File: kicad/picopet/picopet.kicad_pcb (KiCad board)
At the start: 2 copper layers, 11 parts, among them J1 USB_C_Receptacle_G-Switch_GT-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, U2 W25Q128JVS, U3 RP2040, Y1 ABLS-12.000MHZ-B4-T

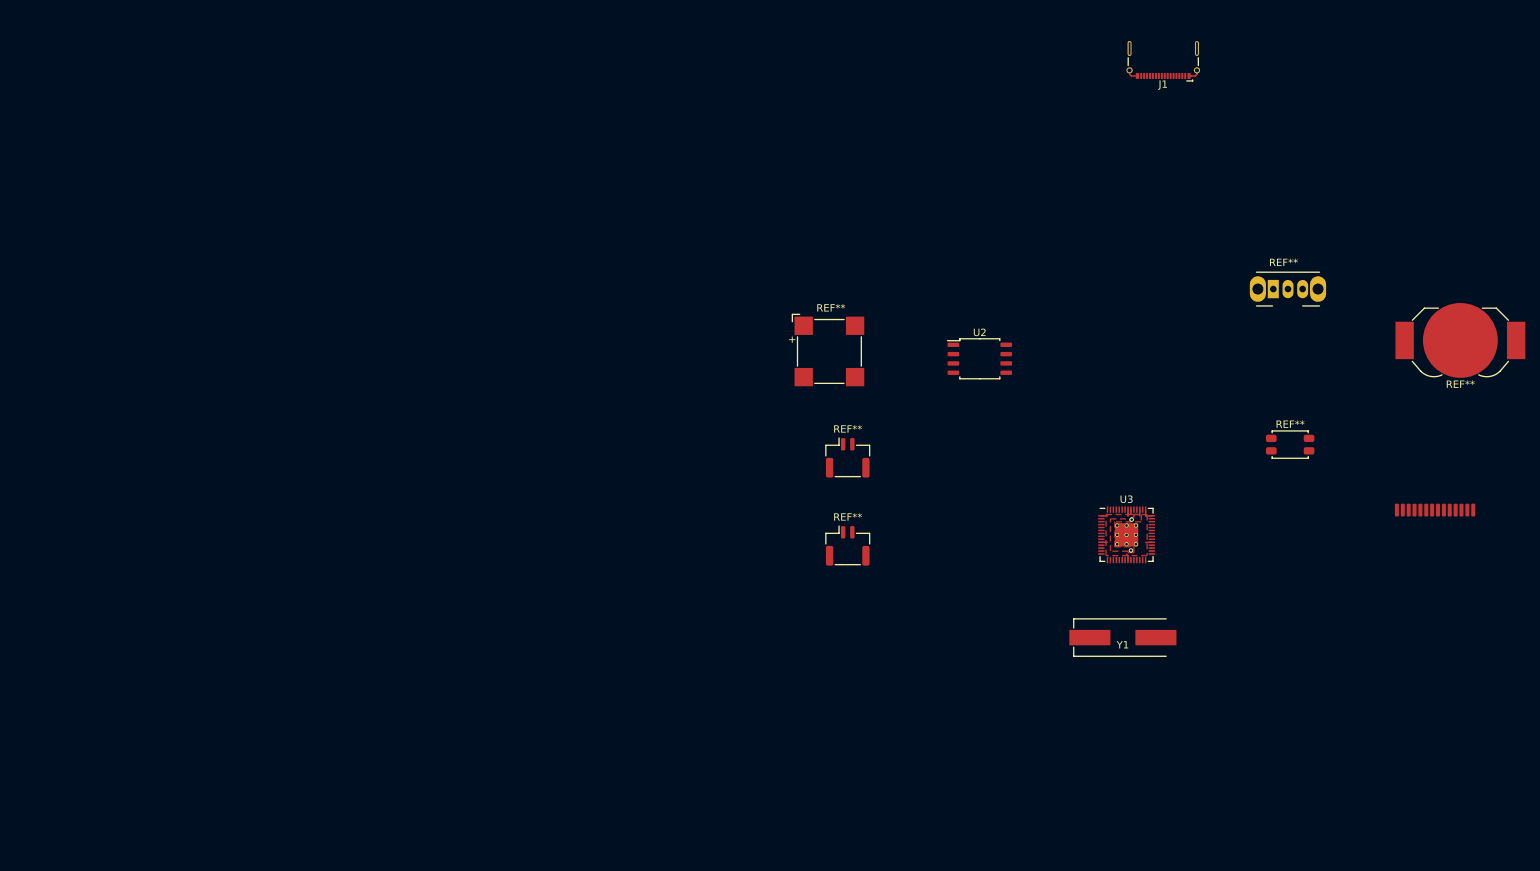
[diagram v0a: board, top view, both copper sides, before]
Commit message: Working on a PCB layout, but didn't plan the LCD well enough
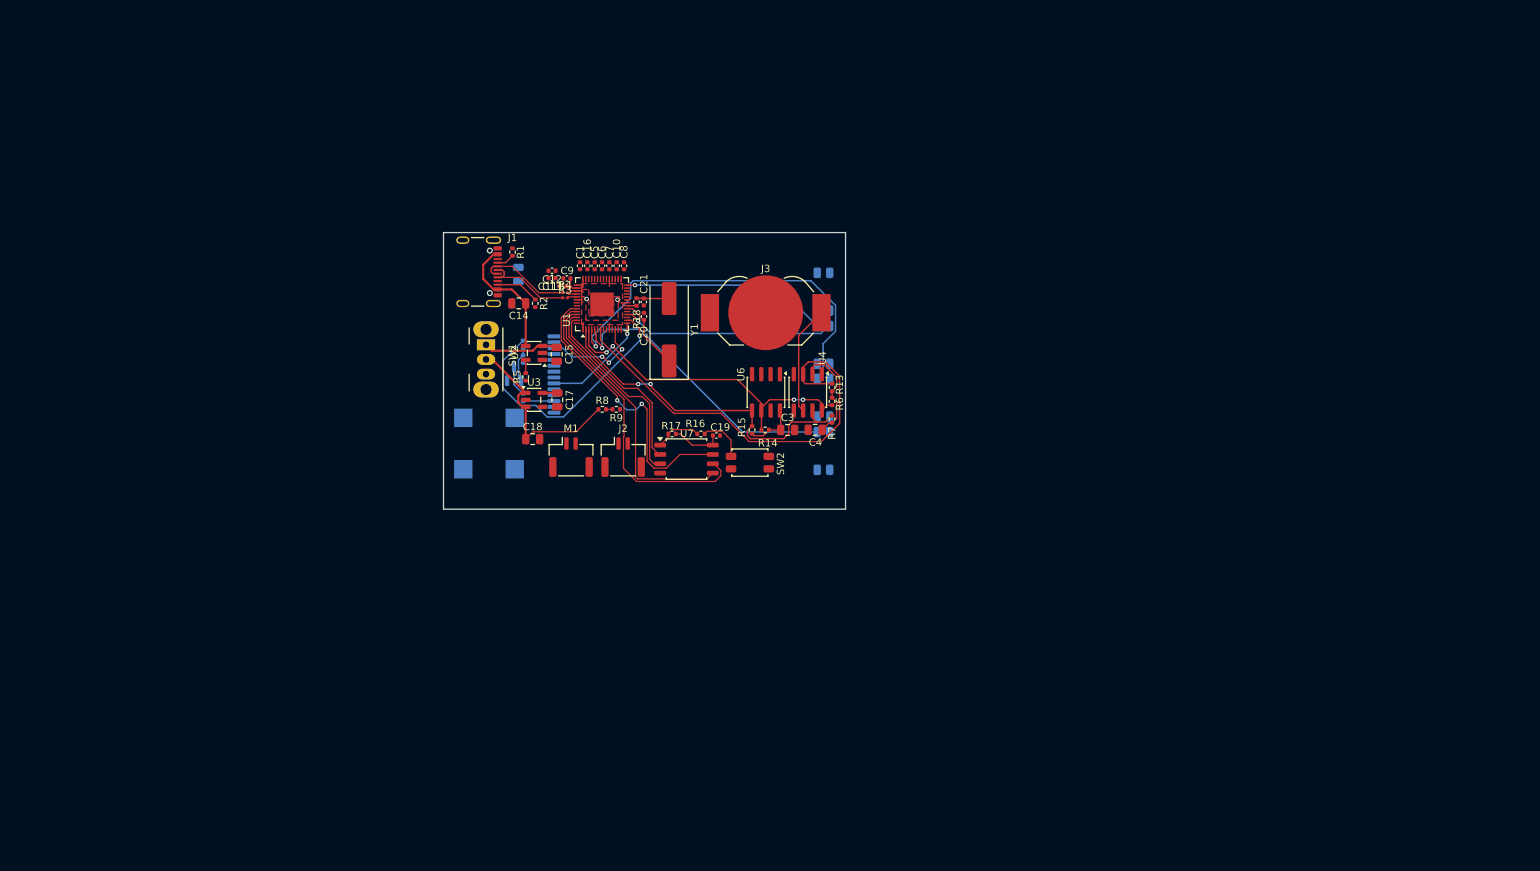
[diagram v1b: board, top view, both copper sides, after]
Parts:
- removed REF** (x2): JST_GH_SM02B-GHS-TB_1x02-1MP_P1.25mm_Horizontal, Connector_JST:JST_GH_SM02B-GHS-TB_1x02-1MP_P1.25mm_Horizontal
- removed REF**: ST7735_P0.8mm, custom:ST7735_P0.8mm
- removed REF**: MagneticBuzzer_CUI_CMT-8504-100-SMT, Buzzer_Beeper:MagneticBuzzer_CUI_CMT-8504-100-SMT
- removed REF**: SW_Slide_SPDT_Angled_CK_OS102011MA1Q, Button_Switch_THT:SW_Slide_SPDT_Angled_CK_OS102011MA1Q
- removed REF**: SW_SPST_EVQP2_MiddlePushTravel_H2.5mm, Button_Switch_SMD:SW_SPST_EVQP2_MiddlePushTravel_H2.5mm
- removed REF**: BatteryHolder_LINX_BAT-HLD-012-SMT, Battery:BatteryHolder_LINX_BAT-HLD-012-SMT
- added BZ1: Buzzer, Buzzer_Beeper:MagneticBuzzer_CUI_CMT-8504-100-SMT, B.Cu at (78.6, 77.1)
- added C1: 100n, Capacitor_SMD:C_0402_1005Metric, F.Cu at (91.0, 52.8)
- added C10: 100n, Capacitor_SMD:C_0402_1005Metric, F.Cu at (96.0, 52.8)
- added C11: 1u, Capacitor_SMD:C_0402_1005Metric, F.Cu at (88.7, 55.6)
- added C12: 100n, Capacitor_SMD:C_0402_1005Metric, F.Cu at (87.2, 53.5)
- added C13: 100n, Capacitor_SMD:C_0402_1005Metric, F.Cu at (87.2, 54.5)
- added C14: 4.7u, Capacitor_SMD:C_0805_2012Metric, F.Cu at (82.7, 58.0)
- added C15: 4.7u, Capacitor_SMD:C_0805_2012Metric, F.Cu at (87.8, 64.9)
- added C16: 100n, Capacitor_SMD:C_0402_1005Metric, F.Cu at (92.0, 52.8)
- added C17: 1u, Capacitor_SMD:C_0805_2012Metric, F.Cu at (87.9, 71.1)
- added C18: 1u, Capacitor_SMD:C_0805_2012Metric, F.Cu at (84.6, 76.5)
- added C19: 100n, Capacitor_SMD:C_0402_1005Metric, F.Cu at (109.6, 76.0)
- added C2: 1u, Capacitor_SMD:C_0805_2012Metric, B.Cu at (82.6, 54.0)
- added C20: 27p, Capacitor_SMD:C_0402_1005Metric, F.Cu at (99.7, 59.7)
- added C21: 27p, Capacitor_SMD:C_0402_1005Metric, F.Cu at (99.7, 57.8)
- added C3: 4.7u, Capacitor_SMD:C_0805_2012Metric, F.Cu at (119.3, 75.2)
- added C4: 4.7u, Capacitor_SMD:C_0805_2012Metric, F.Cu at (123.1, 75.2)
- added C5: 100n, Capacitor_SMD:C_0402_1005Metric, F.Cu at (93.0, 52.8)
- added C6: 100n, Capacitor_SMD:C_0402_1005Metric, F.Cu at (94.0, 52.8)
- added C7: 100n, Capacitor_SMD:C_0402_1005Metric, F.Cu at (95.0, 52.8)
- added C8: 100n, Capacitor_SMD:C_0402_1005Metric, F.Cu at (97.0, 52.8)
- added C9: 1u, Capacitor_SMD:C_0402_1005Metric, F.Cu at (89.2, 54.6)
- added J2: MicroJST 1.25mm female, Connector_JST:JST_GH_SM02B-GHS-TB_1x02-1MP_P1.25mm_Horizontal, F.Cu at (96.9, 78.9)
- added J3: CR1220 Holder, Battery:BatteryHolder_LINX_BAT-HLD-012-SMT, F.Cu at (116.3, 59.2)
- added J4: ST7735 LCD, custom:ST7735_P0.8mm, B.Cu at (102.1, 67.7)
- added M1: Motor_DC, Connector_JST:JST_GH_SM02B-GHS-TB_1x02-1MP_P1.25mm_Horizontal, F.Cu at (89.8, 78.9)
- added Q1: SS8050, Package_TO_SOT_SMD:SOT-23, B.Cu at (82.0, 67.5)
- added R1: 5K1, Resistor_SMD:R_0402_1005Metric, F.Cu at (81.8, 51.0)
- added R10: 10, Resistor_SMD:R_0402_1005Metric, B.Cu at (83.2, 70.8)
- added R11: 10K, Resistor_SMD:R_0402_1005Metric, B.Cu at (83.2, 65.5)
- added R12: 1K, Resistor_SMD:R_0402_1005Metric, B.Cu at (83.2, 63.5)
- added R13: 5K1, Resistor_SMD:R_0402_1005Metric, F.Cu at (125.4, 69.4)
- added R14: 5K1, Resistor_SMD:R_0402_1005Metric, F.Cu at (116.2, 75.2)
- added R15: 5K1, Resistor_SMD:R_0402_1005Metric, F.Cu at (114.5, 75.2)
- added R16: 1k, Resistor_SMD:R_0402_1005Metric, F.Cu at (107.5, 75.7)
- added R17: DNF, Resistor_SMD:R_0402_1005Metric, F.Cu at (103.5, 75.7)
- added R18: 1k, Resistor_SMD:R_0402_1005Metric, F.Cu at (98.7, 57.8)
- added R2: 5K1, Resistor_SMD:R_0402_1005Metric, F.Cu at (84.9, 57.9)
- added R3: 27, Resistor_SMD:R_0201_0603Metric, F.Cu at (89.0, 57.2)
- added R4: 27, Resistor_SMD:R_0201_0603Metric, F.Cu at (89.0, 56.5)
- added R5: 5K1, Resistor_SMD:R_0402_1005Metric, F.Cu at (83.6, 68.0)
- added R6: 5K1, Resistor_SMD:R_0402_1005Metric, F.Cu at (125.4, 71.3)
- added R7: 5K1, Resistor_SMD:R_0402_1005Metric, F.Cu at (125.4, 73.7)
- added R8: 100k, Resistor_SMD:R_0402_1005Metric, F.Cu at (94.0, 72.4)
- added R9: 100k, Resistor_SMD:R_0402_1005Metric, F.Cu at (95.9, 72.4)
- added SW1: PWR, Button_Switch_THT:SW_Slide_SPDT_Angled_CK_OS102011MA1Q, F.Cu at (78.2, 63.6)
- added SW2: BOOTSEL, Button_Switch_SMD:SW_SPST_EVQP2_MiddlePushTravel_H2.5mm, F.Cu at (114.2, 79.7)
- added SW4: Btn0, Button_Switch_SMD:SW_SPST_EVQP2_MiddlePushTravel_H2.5mm, B.Cu at (124.2, 56.4)
- added SW5: Btn1, Button_Switch_SMD:SW_SPST_EVQP2_MiddlePushTravel_H2.5mm, B.Cu at (124.2, 63.6)
- added SW6: Btn2, Button_Switch_SMD:SW_SPST_EVQP2_MiddlePushTravel_H2.5mm, B.Cu at (124.2, 70.8)
- added SW7: Btn3, Button_Switch_SMD:SW_SPST_EVQP2_MiddlePushTravel_H2.5mm, B.Cu at (124.2, 78.1)
- added U1: RP2040, Package_DFN_QFN:QFN-56-1EP_7x7mm_P0.4mm_EP3.2x3.2mm, F.Cu at (94.0, 58.1)
- added U4: DS3231MZ, Package_SO:SOIC-8_3.9x4.9mm_P1.27mm, F.Cu at (122.1, 70.1)
- added U6: AT24CS32-SSHM, Package_SO:SOIC-8_3.9x4.9mm_P1.27mm, F.Cu at (116.4, 70.1)
- added U7: W25Q128JVS, Package_SO:SOIC-8_5.3x5.3mm_P1.27mm, F.Cu at (105.5, 79.2)
- J1: value USB_C_Receptacle_G-Switch_GT-USB-7025 -> USB_C_Receptacle_USB2.0_14P; footprint Connector_USB:USB_C_Receptacle_G-Switch_GT-USB-7025 -> Connector_USB:USB_C_Receptacle_GCT_USB4105-xx-A_16P_TopMnt_Horizontal
- U2: value W25Q128JVS -> MCP73831-2-OT; footprint Package_SO:SOIC-8_5.23x5.23mm_P1.27mm -> Package_TO_SOT_SMD:SOT-23-5
- U3: value RP2040 -> S-T111B33MC-OGSTFU; footprint RP2040_minimal:RP2040-QFN-56 -> Package_TO_SOT_SMD:SOT-23-5
- Y1: footprint RP2040_minimal:Crystal_SMD_HC49-US -> Crystal:Crystal_SMD_HC49-SD
- moved J1 99.1 mm to (76.1, 53.7), turned to -90 degrees
- moved U3 82.8 mm to (84.7, 71.1)
- moved Y1 74.7 mm to (103.2, 61.5), turned to 90 degrees
- moved U2 60.8 mm to (84.7, 64.7), turned to 180 degrees
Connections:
- J1 pad A1: (no net) -> GND
- J1 pad A12: (no net) -> GND
- J1 pad A4: (no net) -> Net-(U2-V_{DD})
- J1 pad A5: (no net) -> Net-(J1-CC1)
- J1 pad A6: (no net) -> USB_D+
- J1 pad A7: (no net) -> USB_D-
- J1 pad A9: (no net) -> Net-(U2-V_{DD})
- J1 pad B1: (no net) -> GND
- J1 pad B12: (no net) -> GND
- J1 pad B4: (no net) -> Net-(U2-V_{DD})
- J1 pad B5: (no net) -> Net-(J1-CC2)
- J1 pad B6: (no net) -> USB_D+
- J1 pad B7: (no net) -> USB_D-
- J1 pad B9: (no net) -> Net-(U2-V_{DD})
- J1 pad S1: (no net) -> GND
- U2 pad 1: (no net) -> GPIO_UNDECIDE_A
- U2 pad 2: (no net) -> GND
- U2 pad 3: (no net) -> VBAT
- U2 pad 4: (no net) -> Net-(U2-V_{DD})
- U2 pad 5: (no net) -> Net-(U2-PROG)
- U3 pad 1: (no net) -> VSENSE
- U3 pad 2: (no net) -> GND
- U3 pad 3: (no net) -> VSENSE
- U3 pad 4: (no net) -> GND
- U3 pad 5: (no net) -> +3V3
- Y1 pad 1: (no net) -> /XIN
- Y1 pad 2: (no net) -> Net-(C21-Pad1)
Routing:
- net GPIO5: track 0.00 -> 59.3 mm
- net GPIO2: track 0.00 -> 54.1 mm, vias 0 -> 1
- net GPIO0: track 0.00 -> 48.1 mm, vias 0 -> 2
- net GPIO1: track 0.00 -> 45.3 mm, vias 0 -> 4
- net /QSPI_SCLK: track 0.00 -> 42.5 mm
- net GPIO3: track 0.00 -> 40.2 mm, vias 0 -> 1
- net /QSPI_SD3: track 0.00 -> 39.5 mm, vias 0 -> 2
- net /QSPI_SD0: track 0.00 -> 38.0 mm
- net GPIO13: track 0.00 -> 36.0 mm, vias 0 -> 1
- net +3V3: track 6.98 -> 40.0 mm
- net GPIO15: track 0.00 -> 31.0 mm, vias 0 -> 1
- net GPIO17: track 0.00 -> 28.2 mm, vias 0 -> 1
- net /QSPI_SD2: track 0.00 -> 27.5 mm
- net VSENSE: track 0.00 -> 25.7 mm
- net /QSPI_SD1: track 0.00 -> 25.1 mm
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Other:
- board outline added: 54.8 x 37.7 mm

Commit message: Redesigning pcb
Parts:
- removed M1: Motor_DC, Connector_JST:JST_GH_SM02B-GHS-TB_1x02-1MP_P1.25mm_Horizontal
- removed R16, R18: 1k, Resistor_SMD:R_0402_1005Metric
- removed R17: DNF, Resistor_SMD:R_0402_1005Metric
- removed SW7: Btn3, Button_Switch_SMD:SW_SPST_EVQP2_MiddlePushTravel_H2.5mm
- added J5: ST7735 LCD, custom:ST7735_P0.8mm, F.Cu at (115.4, 58.5)
- added SW3: Btn0, Button_Switch_SMD:SW_SPST_EVQP2_MiddlePushTravel_H2.5mm, F.Cu at (105.1, 65.4)
- BZ1, Q1: moved to F.Cu
- C11: value 1u -> 100n
- C12, C13: value 100n -> 15p
- C14, C3, C4: value 4.7u -> 100n; footprint Capacitor_SMD:C_0805_2012Metric -> Capacitor_SMD:C_0402_1005Metric
- C15: value 4.7u -> 2u2; footprint Capacitor_SMD:C_0805_2012Metric -> Capacitor_SMD:C_0402_1005Metric
- C16, C8: value 100n -> 1u
- C19: value 100n -> 4.7u; footprint Capacitor_SMD:C_0402_1005Metric -> Capacitor_SMD:C_0805_2012Metric
- C2: value 1u -> 100n; footprint Capacitor_SMD:C_0805_2012Metric -> Capacitor_SMD:C_0402_1005Metric; moved to F.Cu
- C20, C21: value 27p -> 4.7u; footprint Capacitor_SMD:C_0402_1005Metric -> Capacitor_SMD:C_0805_2012Metric
- J2: value MicroJST 1.25mm female -> PH1.25mm 2P
- J3: value CR1220 Holder -> PH1.25mm 2P; footprint Battery:BatteryHolder_LINX_BAT-HLD-012-SMT -> Connector_JST:JST_GH_SM02B-GHS-TB_1x02-1MP_P1.25mm_Horizontal
- J4: value ST7735 LCD -> CR1220 Holder; footprint custom:ST7735_P0.8mm -> Battery:BatteryHolder_LINX_BAT-HLD-012-SMT; moved to F.Cu
- R1, R2: value 5K1 -> 27; footprint Resistor_SMD:R_0402_1005Metric -> Resistor_SMD:R_0201_0603Metric
- R10: value 10 -> 5k1; footprint Resistor_SMD:R_0402_1005Metric -> Resistor_SMD:R_0201_0603Metric; moved to F.Cu
- R11: value 10K -> 5k1; footprint Resistor_SMD:R_0402_1005Metric -> Resistor_SMD:R_0201_0603Metric; moved to F.Cu
- R12: value 1K -> 5k1; footprint Resistor_SMD:R_0402_1005Metric -> Resistor_SMD:R_0201_0603Metric; moved to F.Cu
- R13, R14, R15: footprint Resistor_SMD:R_0402_1005Metric -> Resistor_SMD:R_0201_0603Metric
- R3: value 27 -> 1k; footprint Resistor_SMD:R_0201_0603Metric -> Resistor_SMD:R_0402_1005Metric
- R4: value 27 -> 1k
- R5: value 5K1 -> 10; footprint Resistor_SMD:R_0402_1005Metric -> Resistor_SMD:R_0201_0603Metric
- R6: value 5K1 -> 10k; footprint Resistor_SMD:R_0402_1005Metric -> Resistor_SMD:R_0201_0603Metric
- R7: value 5K1 -> 1k; footprint Resistor_SMD:R_0402_1005Metric -> Resistor_SMD:R_0201_0603Metric
- SW1: footprint Button_Switch_THT:SW_Slide_SPDT_Angled_CK_OS102011MA1Q -> Button_Switch_SMD:SW_SPDT_CK_JS102011SAQN
- SW4: value Btn0 -> Btn1; moved to F.Cu
- SW5: value Btn1 -> Btn2; moved to F.Cu
- SW6: value Btn2 -> Btn3; moved to F.Cu
- U7: value W25Q128JVS -> W25Q32JVSSIQ; footprint Package_SO:SOIC-8_5.3x5.3mm_P1.27mm -> Package_SO:SOIC-8-1EP_3.9x4.9mm_P1.27mm_EP2.29x3mm
- Y1: value ABLS-12.000MHZ-B4-T -> X322512MSB4SI; footprint Crystal:Crystal_SMD_HC49-SD -> Crystal:Crystal_SMD_3225-4Pin_3.2x2.5mm
- moved C4 99.4 mm to (28.0, 46.0), turned to 0 degrees
- moved C3 95.0 mm to (27.5, 50.5)
- moved C20 89.3 mm to (36.1, 122.4), turned to 180 degrees
- moved C19 89.3 mm to (32.8, 121.5), turned to -90 degrees
- moved J4 88.7 mm to (179.1, 23.7), turned to 0 degrees
- moved SW2 87.7 mm to (30.6, 52.8), turned to 90 degrees
- moved J1 83.1 mm to (39.5, 128.3), turned to 0 degrees
- moved SW1 82.0 mm to (29.0, 129.2), turned to 0 degrees
- moved J2 80.4 mm to (28.4, 121.1), turned to -90 degrees
- moved R9 77.7 mm to (28.9, 111.6)
- moved R8 77.7 mm to (27.0, 111.6)
- moved C8 77.2 mm to (19.8, 52.1), turned to -90 degrees
- moved C7 77.1 mm to (18.0, 50.5), turned to 180 degrees
- moved C6 76.7 mm to (17.6, 46.0), turned to 180 degrees
- moved C10 74.7 mm to (22.2, 41.2)
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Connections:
- net GPIO_UNDECIDE_B renamed GPIO26
- C10 pad 1: +3V3 -> +1V1
- C12 pad 1: +1V1 -> /XIN
- C13 pad 1: +1V1 -> Net-(C13-Pad1)
- C14 pad 1: Net-(U2-V_{DD}) -> +3V3
- C15 pad 1: VBAT -> GND
- C15 pad 2: GND -> +3V3
- C16 pad 1: +3V3 -> GND
- C16 pad 2: GND -> +3V3
- C19 pad 1: +3V3 -> VBAT
- C20 pad 1: /XIN -> USBC_VDD
- C21 pad 1: Net-(C21-Pad1) -> +3V3
- C9 pad 1: +3V3 -> +1V1
- J1 pad A4: Net-(U2-V_{DD}) -> USBC_VDD
- J1 pad A9: Net-(U2-V_{DD}) -> USBC_VDD
- J1 pad B4: Net-(U2-V_{DD}) -> USBC_VDD
- J1 pad B9: Net-(U2-V_{DD}) -> USBC_VDD
- J3 pad 1: VCOIN -> GND
- J3 pad 2: GND -> GPIO6
- J4 pad 1: (no net) -> VCOIN
- R1 pad 1: Net-(J1-CC1) -> USB_D+
- R1 pad 2: GND -> Net-(U1-USB_DP)
- R10 pad 1: Net-(J4-LED-) -> Net-(J1-CC1)
- R10 pad 2: Net-(Q1-C) -> GND
- R11 pad 1: +3V3 -> Net-(J1-CC2)
- R11 pad 2: Net-(Q1-B) -> GND
- R12 pad 1: Net-(Q1-B) -> GND
- R12 pad 2: GPIO13 -> Net-(U2-PROG)
- R2 pad 1: Net-(J1-CC2) -> USB_D-
- R2 pad 2: GND -> Net-(U1-USB_DM)
- R3 pad 1: USB_D+ -> /XOUT
- R3 pad 2: Net-(U1-USB_DP) -> Net-(C13-Pad1)
- R4 pad 1: USB_D- -> /QSPI_SS
- R4 pad 2: Net-(U1-USB_DM) -> Net-(R4-Pad2)
- R5 pad 1: GND -> Net-(Q1-C)
- R5 pad 2: Net-(U2-PROG) -> Net-(J5-LED-)
- R6 pad 1: GPIO1 -> Net-(Q1-B)
- R7 pad 1: GPIO0 -> GPIO13
- R7 pad 2: +3V3 -> Net-(Q1-B)
- SW1 pad 1: VBAT -> VSENSE
- SW1 pad 2: VSENSE -> VBAT
- SW1 pad 3: (no net) -> unconnected-(SW1-C-Pad3)
- SW2 pad 1: GND -> Net-(R4-Pad2)
- SW2 pad 2: Net-(R16-Pad2) -> GND
- SW4 pad 1: GPIO15 -> GPIO17
- SW5 pad 1: GPIO17 -> GPIO2
- SW6 pad 1: GPIO2 -> GPIO3
- U1 pad 37: /GPIO25 -> GPIO25
- U2 pad 1: GPIO_UNDECIDE_A -> GPIO25
- U2 pad 4: Net-(U2-V_{DD}) -> USBC_VDD
- Y1 pad 2: Net-(C21-Pad1) -> Net-(C13-Pad1)
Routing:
- net GPIO5: track 59.3 -> 1.96 mm
- net GPIO2: track 54.1 -> 0.00 mm, vias 1 -> 0
- net GPIO3: track 40.2 -> 0.00 mm, vias 1 -> 0
- net GPIO13: track 36.0 -> 0.00 mm, vias 1 -> 0
- net GPIO0: track 48.1 -> 14.1 mm, vias 2 -> 0
- net GPIO1: track 45.3 -> 11.8 mm, vias 4 -> 0
- net GPIO15: track 31.0 -> 0.00 mm, vias 1 -> 0
- net GPIO17: track 28.2 -> 0.00 mm, vias 1 -> 0
- net /QSPI_SD0: track 38.0 -> 17.5 mm
- net /QSPI_SCLK: track 42.5 -> 22.6 mm
- net +3V3: track 40.0 -> 21.3 mm
- net Net-(U2-V_{DD}): track 17.5 -> 0.00 mm
- net /QSPI_SD2: track 27.5 -> 11.1 mm
- net VCOIN: track 14.9 -> 0.00 mm
- net /QSPI_SD1: track 25.1 -> 10.3 mm
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- removed copper zone on F.Cu, net +1V1
- removed copper zone on F.Cu, net +3V3
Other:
- board outline removed

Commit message: Redesigning pcb
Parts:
- J5, SW3, SW4, SW5, SW6: moved to B.Cu
- U7: footprint Package_SO:SOIC-8-1EP_3.9x4.9mm_P1.27mm_EP2.29x3mm -> Package_SO:SOIC-8_3.9x4.9mm_P1.27mm
- moved Y1 108.7 mm to (27.8, 36.3), turned to 180 degrees
- moved J4 106.1 mm to (75.0, 44.3), turned to 90 degrees
- moved C13 105.9 mm to (25.2, 35.9), turned to -90 degrees
- moved J3 101.7 mm to (33.9, 45.1), turned to 180 degrees
- moved BZ1 100.9 mm to (49.9, 126.9), turned to -90 degrees
- moved R3 99.3 mm to (24.2, 36.0), turned to 90 degrees
- moved C12 98.6 mm to (30.4, 35.9), turned to -90 degrees
- moved C21 95.2 mm to (69.1, 52.2)
- moved R13 95.2 mm to (60.1, 46.1)
- moved R14 95.2 mm to (67.3, 43.5)
- moved R15 95.2 mm to (69.1, 50.1)
- moved U4 95.2 mm to (64.3, 46.4)
- moved U6 95.2 mm to (64.3, 51.9)
- moved C14 91.6 mm to (39.3, 49.0), turned to 180 degrees
- moved C15 91.5 mm to (39.3, 48.0)
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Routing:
- net +3V3: track 21.3 -> 53.6 mm, vias 0 -> 4
- net GND: track 0.43 -> 25.5 mm, vias 0 -> 2
- net VCOIN: track 0.00 -> 15.1 mm
- net +1V1: track 5.49 -> 18.8 mm
- net GPIO0: track 14.1 -> 23.9 mm, vias 0 -> 3
- net GPIO1: track 11.8 -> 20.5 mm, vias 0 -> 3
- net /XIN: track 0.00 -> 4.97 mm
- net /XOUT: track 0.00 -> 3.47 mm
- net GPIO12: track 0.00 -> 2.67 mm, vias 0 -> 2
- net Net-(C13-Pad1): track 0.00 -> 2.50 mm
- net GPIO10: track 0.00 -> 1.70 mm, vias 0 -> 1
- net GPIO11: track 0.00 -> 1.70 mm, vias 0 -> 1
- net GPIO8: track 0.00 -> 1.70 mm, vias 0 -> 1
- net Net-(J5-LED-): track 0.00 -> 1.70 mm, vias 0 -> 1
- net GPIO9: track 0.00 -> 1.70 mm, vias 0 -> 1
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- added copper zone on F.Cu, net +3V3
- added copper zone on F.Cu, net GND

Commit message: Working on mcu layout
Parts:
- moved SW1 55.9 mm to (46.3, 76.0), turned to -90 degrees
- moved R8 52.6 mm to (63.9, 74.1), turned to 90 degrees
- moved J2 52.5 mm to (54.4, 75.5), turned to 180 degrees
- moved U3 52.1 mm to (59.6, 74.7), turned to -90 degrees
- moved C18 52.1 mm to (62.4, 74.5), turned to -90 degrees
- moved R9 49.9 mm to (63.9, 76.0), turned to 90 degrees
- moved C17 47.8 mm to (59.6, 77.7), turned to 180 degrees
- moved C19 46.8 mm to (54.0, 79.8), turned to 180 degrees
- moved C20 42.8 mm to (53.1, 83.1), turned to 90 degrees
- moved J1 42.5 mm to (47.2, 86.5), turned to -90 degrees
- moved U2 41.7 mm to (55.9, 83.0), turned to -90 degrees
- moved R10 40.2 mm to (52.8, 85.2), turned to 0 degrees
- moved R12 39.8 mm to (58.1, 83.8), turned to -90 degrees
- moved R11 36.3 mm to (52.8, 88.2), turned to 0 degrees
- moved BZ1 30.0 mm to (48.6, 96.9), turned to 180 degrees
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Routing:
- net +3V3: track 53.6 -> 79.7 mm, vias 4 -> 9
- net GND: track 25.5 -> 33.4 mm, vias 2 -> 4
- net GPIO6: track 0.00 -> 6.20 mm
- net GPIO8: track 1.70 -> 6.50 mm, vias 1 -> 2
- net GPIO9: track 1.70 -> 5.59 mm, vias 1 -> 2
- net /XIN: track 4.97 -> 8.22 mm
- net GPIO10: track 1.70 -> 4.76 mm, vias 1 -> 2
- net GPIO11: track 1.70 -> 3.69 mm, vias 1 -> 2
- net GPIO0: track 23.9 -> 25.8 mm, vias 3 -> 4
- net GPIO1: track 20.5 -> 22.3 mm, vias 3 -> 4
- net GPIO3: track 0.00 -> 1.75 mm, vias 0 -> 1
- net GPIO2: track 0.00 -> 1.73 mm, vias 0 -> 1
- net GPIO4: track 0.00 -> 1.62 mm, vias 0 -> 1
- net /XOUT: track 3.47 -> 5.07 mm
- net /GPIO26_ADC0: track 0.00 -> 0.98 mm, vias 0 -> 1
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- added copper zone on B.Cu, net +3V3
